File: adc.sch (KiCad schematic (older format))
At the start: 89 parts, among them CN14 10nF, CN17 10nF, CN5 10nF, CN6 10nF, U35 MCP6004, U36 MCP6004, U46 MCP6004, U8 MCP6004

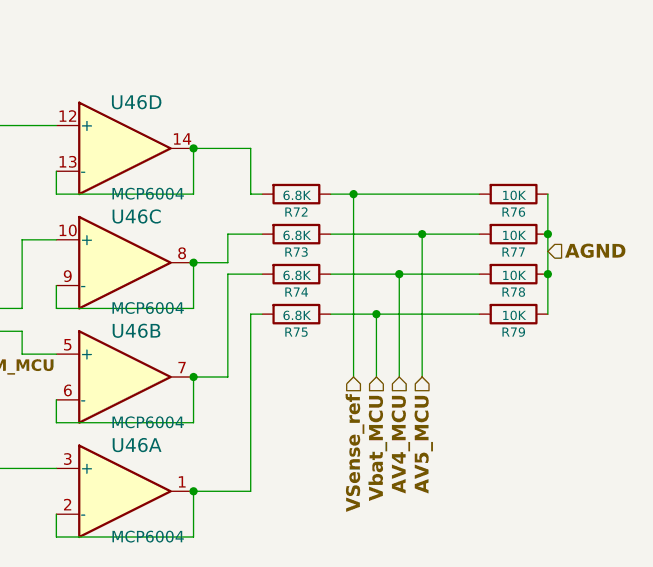
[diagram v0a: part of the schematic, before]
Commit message: Fix mixed up AV4, AV5, 5Vsense, and 12V sense
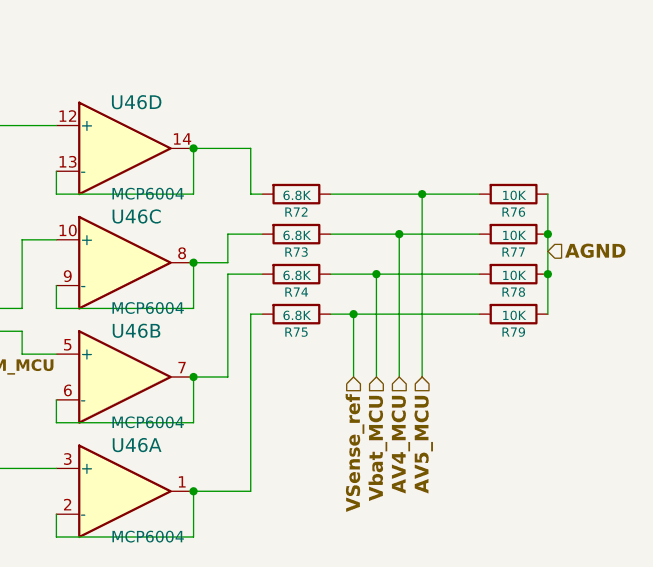
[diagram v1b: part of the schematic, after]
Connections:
- net AV4_MCU: now also R73.1, R77.2; no longer R74.1, R78.2
- net AV5_MCU: now also R72.1, R76.2; no longer R73.1, R77.2
- net VSense_ref: now also R75.1, R79.2; no longer R72.1, R76.2
- net Vbat_MCU: now also R74.1, R78.2; no longer R75.1, R79.2
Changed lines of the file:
@@
 	14200 3525 14200 4300
 Wire Wire Line
-	14550 3525 14750 3525
-Wire Wire Line
-	14550 3350 14850 3350
-Wire Wire Line
-	14550 3175 14950 3175
-Wire Wire Line
-	14550 3000 14650 3000
+	14550 3525 14650 3525
+Wire Wire Line
+	14550 3350 14750 3350
+Wire Wire Line
+	14550 3175 14850 3175
 Wire Wire Line
 	15500 3000 15500 3175
@@
 Wire Wire Line
 	15500 3350 15500 3525
-Wire Wire Line
-	14650 3800 14650 3000
-Connection ~ 14650 3000
-Wire Wire Line
-	14650 3000 15200 3000
-Wire Wire Line
-	14750 3800 14750 3525
-Connection ~ 14750 3525
-Wire Wire Line
-	14750 3525 15200 3525
-Wire Wire Line
-	14850 3800 14850 3350
-Connection ~ 14850 3350
-Wire Wire Line
-	14850 3350 15200 3350
-Wire Wire Line
-	14950 3800 14950 3175
-Connection ~ 14950 3175
-Wire Wire Line
-	14950 3175 15200 3175
 $Comp
 L Power_Protection:NUP4202 D40
@@
 Wire Wire Line
 	2050 8275 2050 8350
+Wire Wire Line
+	14650 3800 14650 3525
+Connection ~ 14650 3525
+Wire Wire Line
+	14650 3525 15200 3525
+Wire Wire Line
+	14750 3800 14750 3350
+Connection ~ 14750 3350
+Wire Wire Line
+	14750 3350 15200 3350
+Wire Wire Line
+	14850 3800 14850 3175
+Connection ~ 14850 3175
+Wire Wire Line
+	14850 3175 15200 3175
+Wire Wire Line
+	14950 3800 14950 3000
+Wire Wire Line
+	14550 3000 14950 3000
+Connection ~ 14950 3000
+Wire Wire Line
+	14950 3000 15200 3000
 $EndSCHEMATC
